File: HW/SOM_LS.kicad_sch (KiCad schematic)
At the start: 1 part

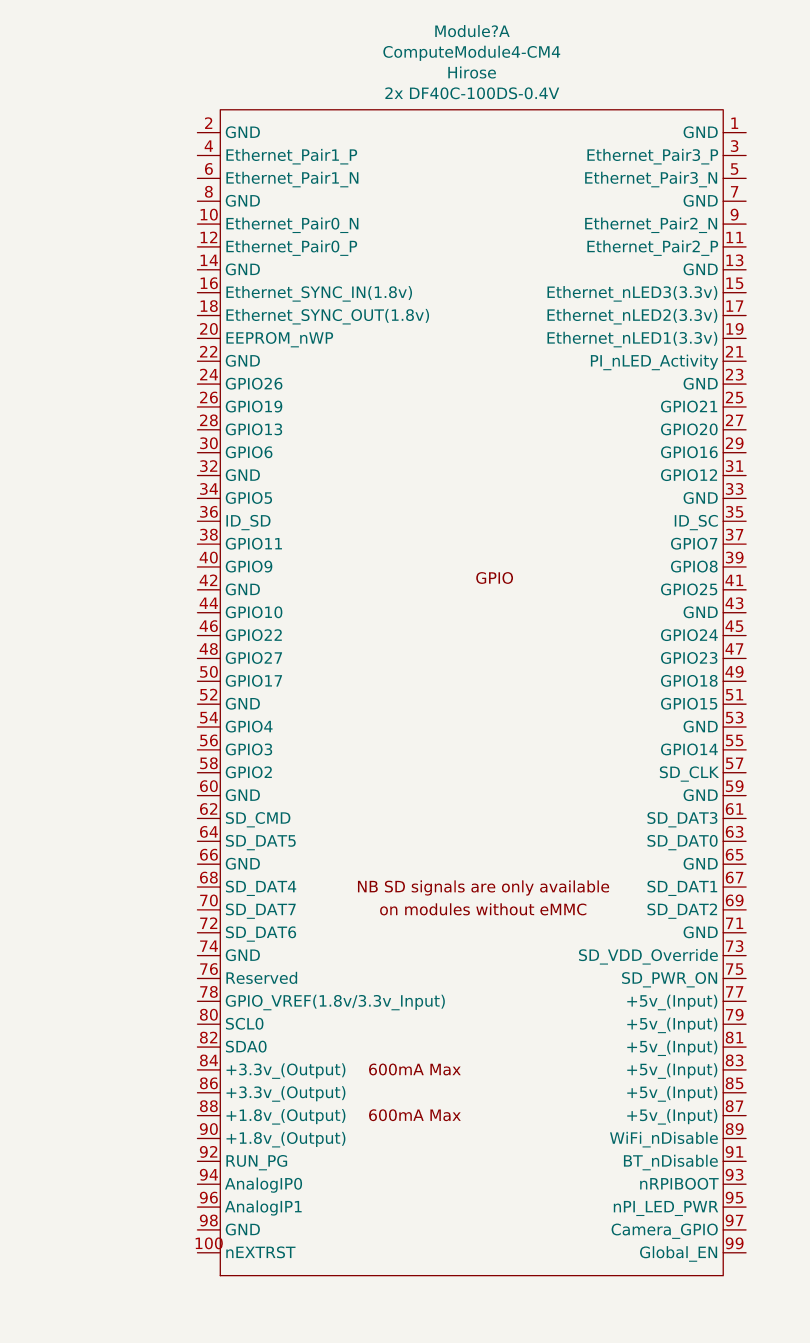
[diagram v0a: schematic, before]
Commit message: added gnds, some connector breakout
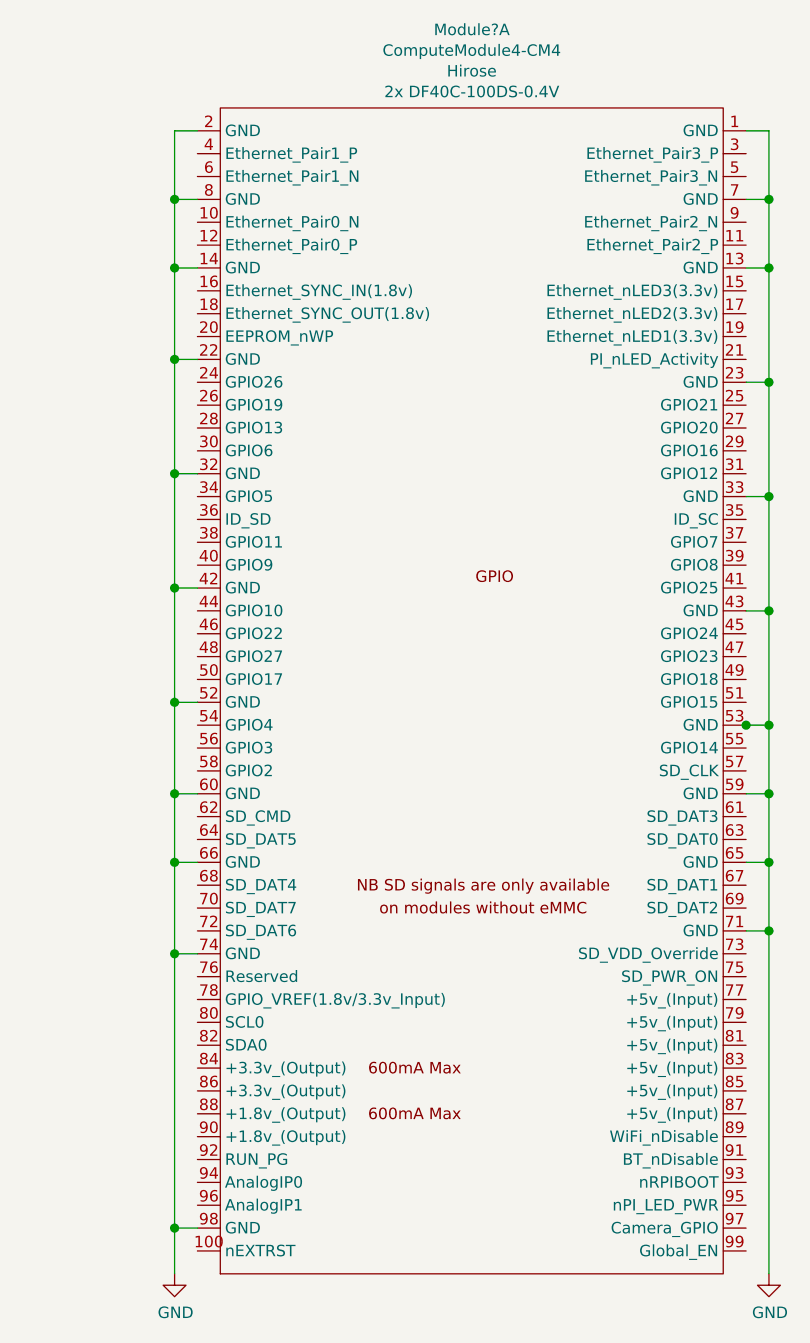
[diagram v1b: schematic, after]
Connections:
- net GND: now reaches Module?.1 (GND)
- net GND: now also Module?.13 (GND), Module?.14 (GND), Module?.2 (GND), Module?.22 (GND), Module?.23 (GND), Module?.32 (GND), Module?.33 (GND), Module?.42 (GND), Module?.43 (GND), Module?.52 (GND), Module?.53 (GND), Module?.59 (GND), Module?.60 (GND), Module?.65 (GND), Module?.66 (GND), Module?.7 (GND), Module?.71 (GND), Module?.74 (GND), Module?.8 (GND), Module?.98 (GND)
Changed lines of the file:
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@@
   (page 1 6)
   (paper "B")
-  (symbol (lib_id "CM4IO:ComputeModule4-CM4") (at 118.11 105.6132 0) (unit 1)
+  (junction (at 82.55 57.15) (diameter 1.016) (color 0 0 0 0))
+  (junction (at 82.55 64.77) (diameter 1.016) (color 0 0 0 0))
+  (junction (at 82.55 74.93) (diameter 1.016) (color 0 0 0 0))
+  (junction (at 82.55 87.63) (diameter 1.016) (color 0 0 0 0))
+  (junction (at 82.55 100.33) (diameter 1.016) (color 0 0 0 0))
+  (junction (at 82.55 113.03) (diameter 1.016) (color 0 0 0 0))
+  (junction (at 82.55 123.19) (diameter 1.016) (color 0 0 0 0))
+  (junction (at 82.55 130.81) (diameter 1.016) (color 0 0 0 0))
+  (junction (at 82.55 140.97) (diameter 1.016) (color 0 0 0 0))
+  (junction (at 82.55 171.45) (diameter 1.016) (color 0 0 0 0))
+  (junction (at 146.05 115.57) (diameter 1.016) (color 0 0 0 0))
+  (junction (at 148.59 57.15) (diameter 1.016) (color 0 0 0 0))
+  (junction (at 148.59 64.77) (diameter 1.016) (color 0 0 0 0))
+  (junction (at 148.59 77.47) (diameter 1.016) (color 0 0 0 0))
+  (junction (at 148.59 90.17) (diameter 1.016) (color 0 0 0 0))
+  (junction (at 148.59 102.87) (diameter 1.016) (color 0 0 0 0))
+  (junction (at 148.59 115.57) (diameter 1.016) (color 0 0 0 0))
+  (junction (at 148.59 123.19) (diameter 1.016) (color 0 0 0 0))
+  (junction (at 148.59 130.81) (diameter 1.016) (color 0 0 0 0))
+  (junction (at 148.59 138.43) (diameter 1.016) (color 0 0 0 0))
+  (wire (pts (xy 82.55 49.53) (xy 82.55 57.15))
+    (stroke (width 0) (type solid) (color 0 0 0 0))
+  )
+  (wire (pts (xy 82.55 57.15) (xy 82.55 64.77))
+    (stroke (width 0) (type solid) (color 0 0 0 0))
+  )
+  (wire (pts (xy 82.55 64.77) (xy 82.55 74.93))
+    (stroke (width 0) (type solid) (color 0 0 0 0))
+  )
+  (wire (pts (xy 82.55 74.93) (xy 82.55 87.63))
+    (stroke (width 0) (type solid) (color 0 0 0 0))
+  )
+  (wire (pts (xy 82.55 87.63) (xy 82.55 100.33))
+    (stroke (width 0) (type solid) (color 0 0 0 0))
+  )
+  (wire (pts (xy 82.55 87.63) (xy 85.09 87.63))
+    (stroke (width 0) (type solid) (color 0 0 0 0))
+  )
+  (wire (pts (xy 82.55 100.33) (xy 82.55 113.03))
+    (stroke (width 0) (type solid) (color 0 0 0 0))
+  )
+  (wire (pts (xy 82.55 113.03) (xy 82.55 123.19))
+    (stroke (width 0) (type solid) (color 0 0 0 0))
+  )
+  (wire (pts (xy 82.55 123.19) (xy 82.55 130.81))
+    (stroke (width 0) (type solid) (color 0 0 0 0))
+  )
+  (wire (pts (xy 82.55 130.81) (xy 82.55 140.97))
+    (stroke (width 0) (type solid) (color 0 0 0 0))
+  )
+  (wire (pts (xy 82.55 130.81) (xy 85.09 130.81))
+    (stroke (width 0) (type solid) (color 0 0 0 0))
+  )
+  (wire (pts (xy 82.55 140.97) (xy 82.55 171.45))
+    (stroke (width 0) (type solid) (color 0 0 0 0))
+  )
+  (wire (pts (xy 82.55 140.97) (xy 85.09 140.97))
+    (stroke (width 0) (type solid) (color 0 0 0 0))
+  )
+  (wire (pts (xy 82.55 171.45) (xy 82.55 176.53))
+    (stroke (width 0) (type solid) (color 0 0 0 0))
+  )
+  (wire (pts (xy 85.09 49.53) (xy 82.55 49.53))
+    (stroke (width 0) (type solid) (color 0 0 0 0))
+  )
+  (wire (pts (xy 85.09 57.15) (xy 82.55 57.15))
+    (stroke (width 0) (type solid) (color 0 0 0 0))
+  )
+  (wire (pts (xy 85.09 64.77) (xy 82.55 64.77))
+    (stroke (width 0) (type solid) (color 0 0 0 0))
+  )
+  (wire (pts (xy 85.09 74.93) (xy 82.55 74.93))
+    (stroke (width 0) (type solid) (color 0 0 0 0))
+  )
+  (wire (pts (xy 85.09 100.33) (xy 82.55 100.33))
+    (stroke (width 0) (type solid) (color 0 0 0 0))
+  )
+  (wire (pts (xy 85.09 113.03) (xy 82.55 113.03))
+    (stroke (width 0) (type solid) (color 0 0 0 0))
+  )
+  (wire (pts (xy 85.09 123.19) (xy 82.55 123.19))
+    (stroke (width 0) (type solid) (color 0 0 0 0))
+  )
+  (wire (pts (xy 85.09 171.45) (xy 82.55 171.45))
+    (stroke (width 0) (type solid) (color 0 0 0 0))
+  )
+  (wire (pts (xy 146.05 49.53) (xy 148.59 49.53))
+    (stroke (width 0) (type solid) (color 0 0 0 0))
+  )
+  (wire (pts (xy 146.05 57.15) (xy 148.59 57.15))
+    (stroke (width 0) (type solid) (color 0 0 0 0))
+  )
+  (wire (pts (xy 146.05 64.77) (xy 148.59 64.77))
+    (stroke (width 0) (type solid) (color 0 0 0 0))
+  )
+  (wire (pts (xy 146.05 77.47) (xy 148.59 77.47))
+    (stroke (width 0) (type solid) (color 0 0 0 0))
+  )
+  (wire (pts (xy 146.05 90.17) (xy 148.59 90.17))
+    (stroke (width 0) (type solid) (color 0 0 0 0))
+  )
+  (wire (pts (xy 146.05 102.87) (xy 148.59 102.87))
+    (stroke (width 0) (type solid) (color 0 0 0 0))
+  )
+  (wire (pts (xy 146.05 115.57) (xy 146.05 115.7732))
+    (stroke (width 0) (type solid) (color 0 0 0 0))
+  )
+  (wire (pts (xy 146.05 115.57) (xy 148.59 115.57))
+    (stroke (width 0) (type solid) (color 0 0 0 0))
+  )
+  (wire (pts (xy 146.05 123.19) (xy 148.59 123.19))
+    (stroke (width 0) (type solid) (color 0 0 0 0))
+  )
+  (wire (pts (xy 146.05 130.81) (xy 148.59 130.81))
+    (stroke (width 0) (type solid) (color 0 0 0 0))
+  )
+  (wire (pts (xy 146.05 138.43) (xy 148.59 138.43))
+    (stroke (width 0) (type solid) (color 0 0 0 0))
+  )
+  (wire (pts (xy 148.59 49.53) (xy 148.59 57.15))
+    (stroke (width 0) (type solid) (color 0 0 0 0))
+  )
+  (wire (pts (xy 148.59 57.15) (xy 148.59 64.77))
+    (stroke (width 0) (type solid) (color 0 0 0 0))
+  )
+  (wire (pts (xy 148.59 64.77) (xy 148.59 77.47))
+    (stroke (width 0) (type solid) (color 0 0 0 0))
+  )
+  (wire (pts (xy 148.59 77.47) (xy 148.59 90.17))
+    (stroke (width 0) (type solid) (color 0 0 0 0))
+  )
+  (wire (pts (xy 148.59 90.17) (xy 148.59 102.87))
+    (stroke (width 0) (type solid) (color 0 0 0 0))
+  )
+  (wire (pts (xy 148.59 102.87) (xy 148.59 115.57))
+    (stroke (width 0) (type solid) (color 0 0 0 0))
+  )
+  (wire (pts (xy 148.59 115.57) (xy 148.59 123.19))
+    (stroke (width 0) (type solid) (color 0 0 0 0))
+  )
+  (wire (pts (xy 148.59 123.19) (xy 148.59 130.81))
+    (stroke (width 0) (type solid) (color 0 0 0 0))
+  )
+  (wire (pts (xy 148.59 130.81) (xy 148.59 138.43))
+    (stroke (width 0) (type solid) (color 0 0 0 0))
+  )
+  (wire (pts (xy 148.59 138.43) (xy 148.59 176.53))
+    (stroke (width 0) (type solid) (color 0 0 0 0))
+  )
+  (symbol (lib_id "power:GND") (at 82.55 176.53 0) (unit 1)
     (in_bom yes) (on_board yes)
-    (property "Reference" "Module?" (id 0) (at 115.57 38.5126 0))
-    (property "Value" "ComputeModule4-CM4" (id 1) (at 115.57 40.8113 0))
-    (property "Footprint" "CM4IO:Raspberry-Pi-4-Compute-Module" (id 2) (at 260.35 132.2832 0)
+    (property "Reference" "#PWR?" (id 0) (at 82.55 182.88 0)
       (effects (font (size 1.27 1.27)) hide)
     )
-    (property "Datasheet" "" (id 3) (at 260.35 132.2832 0)
+    (property "Value" "GND" (id 1) (at 82.6643 180.8544 0))
+    (property "Footprint" "" (id 2) (at 82.55 176.53 0)
       (effects (font (size 1.27 1.27)) hide)
     )
-    (property "Field4" "Hirose" (id 4) (at 115.57 43.11 0))
-    (property "Field5" "2x DF40C-100DS-0.4V" (id 5) (at 115.57 45.4087 0))
+    (property "Datasheet" "" (id 3) (at 82.55 176.53 0)
+      (effects (font (size 1.27 1.27)) hide)
+    )
+  )
+  (symbol (lib_id "power:GND") (at 148.59 176.53 0) (unit 1)
+    (in_bom yes) (on_board yes)
+    (property "Reference" "#PWR?" (id 0) (at 148.59 182.88 0)
+      (effects (font (size 1.27 1.27)) hide)
+    )
+    (property "Value" "GND" (id 1) (at 148.7043 180.8544 0))
+    (property "Footprint" "" (id 2) (at 148.59 176.53 0)
+      (effects (font (size 1.27 1.27)) hide)
+    )
+    (property "Datasheet" "" (id 3) (at 148.59 176.53 0)
+      (effects (font (size 1.27 1.27)) hide)
+    )
+  )
+  (symbol (lib_id "CM4IO:ComputeModule4-CM4") (at 118.11 105.41 0) (unit 1)
+    (in_bom yes) (on_board yes)
+    (property "Reference" "Module?" (id 0) (at 115.57 38.3094 0))
+    (property "Value" "ComputeModule4-CM4" (id 1) (at 115.57 40.6081 0))
+    (property "Footprint" "CM4IO:Raspberry-Pi-4-Compute-Module" (id 2) (at 260.35 132.08 0)
+      (effects (font (size 1.27 1.27)) hide)
+    )
+    (property "Datasheet" "" (id 3) (at 260.35 132.08 0)
+      (effects (font (size 1.27 1.27)) hide)
+    )
+    (property "Field4" "Hirose" (id 4) (at 115.57 42.9068 0))
+    (property "Field5" "2x DF40C-100DS-0.4V" (id 5) (at 115.57 45.2055 0))
   )
 )

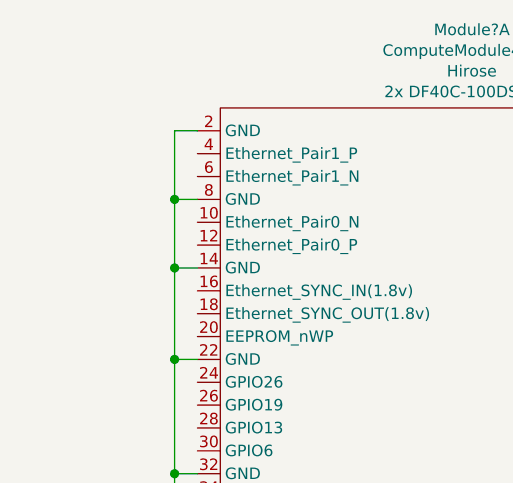
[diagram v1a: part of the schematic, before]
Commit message: More work on USB, added Enet jack
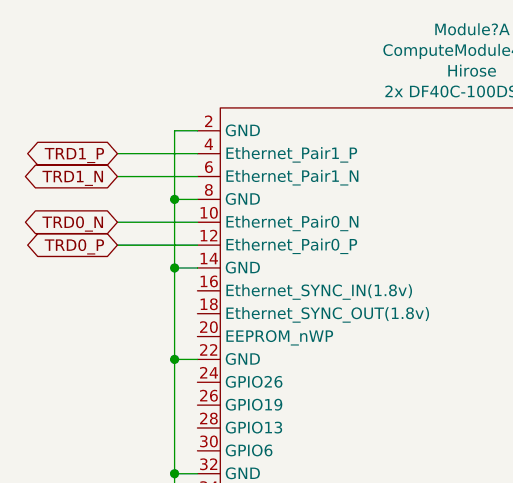
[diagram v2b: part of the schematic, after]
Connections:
- net TRD0_N: now reaches Module?.10 (Ethernet_Pair0_N)
- net TRD0_P: now reaches Module?.12 (Ethernet_Pair0_P)
- net TRD1_P: now reaches Module?.4 (Ethernet_Pair1_P)
- net TRD1_N: now reaches Module?.6 (Ethernet_Pair1_N)
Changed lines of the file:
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@@
   (junction (at 148.59 130.81) (diameter 1.016) (color 0 0 0 0))
   (junction (at 148.59 138.43) (diameter 1.016) (color 0 0 0 0))
+  (wire (pts (xy 76.2 52.07) (xy 85.09 52.07))
+    (stroke (width 0) (type solid) (color 0 0 0 0))
+  )
+  (wire (pts (xy 76.2 54.61) (xy 85.09 54.61))
+    (stroke (width 0) (type solid) (color 0 0 0 0))
+  )
+  (wire (pts (xy 76.2 59.69) (xy 85.09 59.69))
+    (stroke (width 0) (type solid) (color 0 0 0 0))
+  )
+  (wire (pts (xy 76.2 62.23) (xy 85.09 62.23))
+    (stroke (width 0) (type solid) (color 0 0 0 0))
+  )
   (wire (pts (xy 82.55 49.53) (xy 82.55 57.15))
     (stroke (width 0) (type solid) (color 0 0 0 0))
@@
     (stroke (width 0) (type solid) (color 0 0 0 0))
   )
+  (global_label "TRD1_P" (shape bidirectional) (at 76.2 52.07 180)
+    (effects (font (size 1.27 1.27)) (justify right))
+  )
+  (global_label "TRD1_N" (shape bidirectional) (at 76.2 54.61 180)
+    (effects (font (size 1.27 1.27)) (justify right))
+  )
+  (global_label "TRD0_N" (shape bidirectional) (at 76.2 59.69 180)
+    (effects (font (size 1.27 1.27)) (justify right))
+  )
+  (global_label "TRD0_P" (shape bidirectional) (at 76.2 62.23 180)
+    (effects (font (size 1.27 1.27)) (justify right))
+  )
   (symbol (lib_id "power:GND") (at 82.55 176.53 0) (unit 1)
